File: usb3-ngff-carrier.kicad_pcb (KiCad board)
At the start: 4 copper layers, 90 x 40 mm, 51 parts, among them J1 692221030100, J2 2199119-3, J3 Jack-DC, J4 693043020611, J5 Conn_01x03_Male, SW1 KMR221GLFS, U1 TPS82130SILR

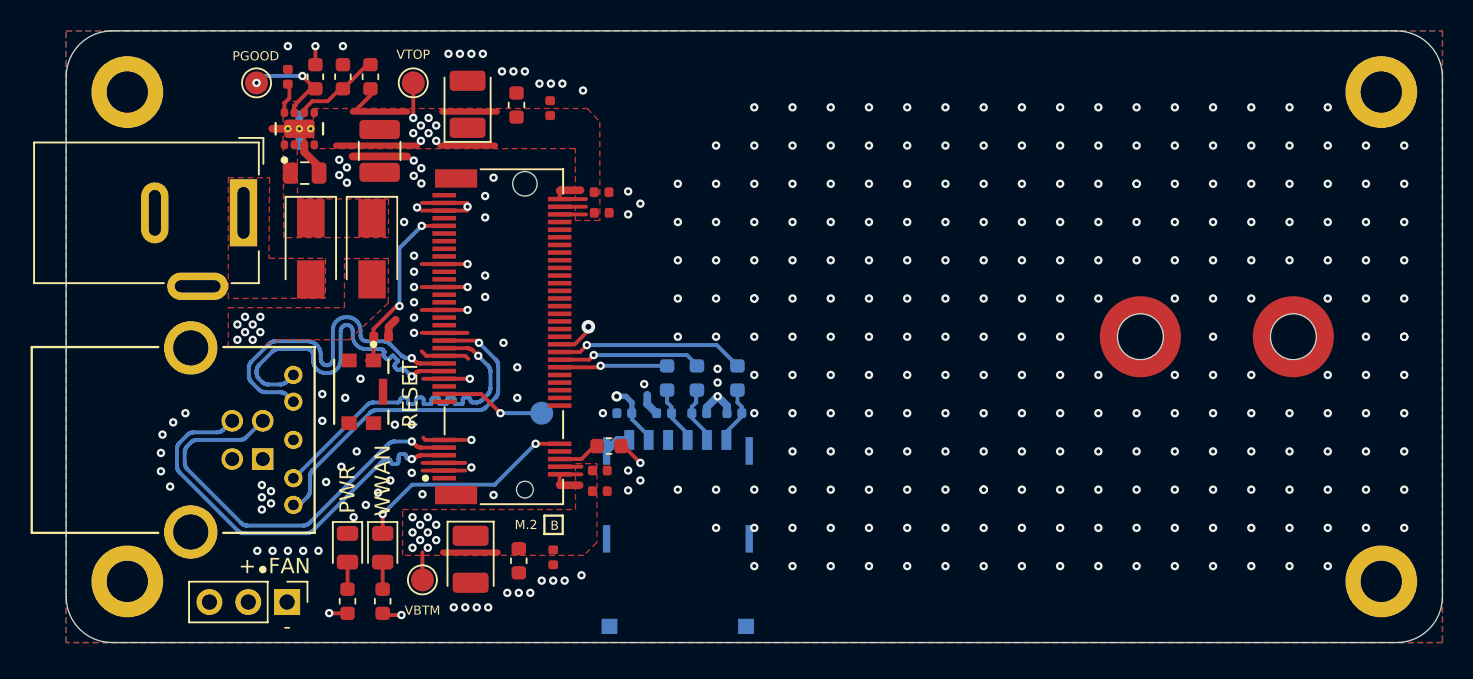
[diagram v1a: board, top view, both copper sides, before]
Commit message: Add: Rev2 changes
* Changed switcher to Diodes Inc device.
* Added second USIM slot and changed USIM slot part.
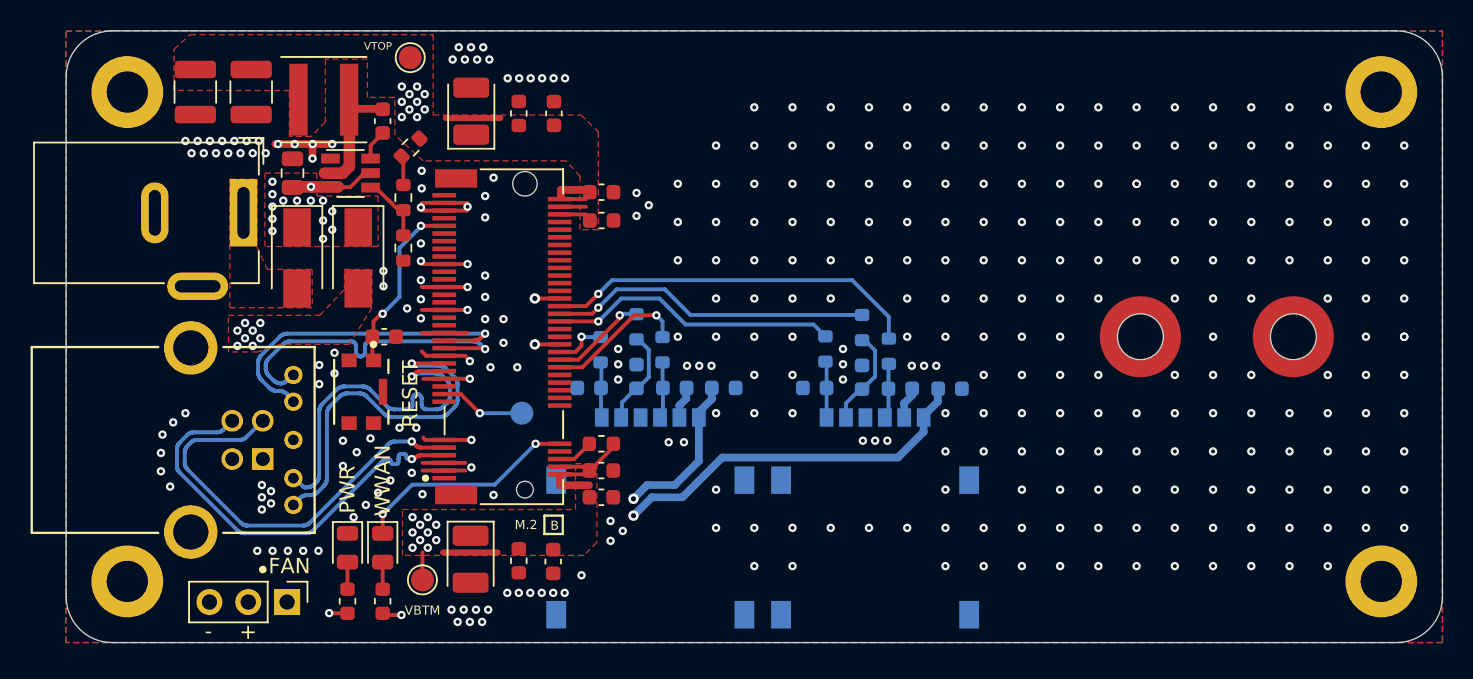
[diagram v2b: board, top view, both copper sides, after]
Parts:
- removed TP3: PGOOD, TestPoint:TestPoint_Pad_D1.5mm
- added C15: 22uF, Capacitor_SMD:C_1210_3225Metric, F.Cu at (12.1, 4.00)
- added C20: 100nF, Capacitor_SMD:C_0603_1608Metric, B.Cu at (43.0, 23.4)
- added C21: 33pF, Capacitor_SMD:C_0603_1608Metric, B.Cu at (39.8, 23.4)
- added C22: 33pF, Capacitor_SMD:C_0603_1608Metric, B.Cu at (37.3, 22.6)
- added C23: 33pF, Capacitor_SMD:C_0603_1608Metric, B.Cu at (34.2, 23.4)
- added J6: SIM8060-6-1-14-00-A, footprint:GCT_SIM8060-6-1-14-00-A, B.Cu at (52.9, 32.1)
- added L1: 3.3uH, Inductor_SMD:L_Coilcraft_XAL5030, F.Cu at (16.9, 4.50)
- added R10: 22R, Resistor_SMD:R_0603_1608Metric, B.Cu at (39.0, 20.9)
- added R11: 22R, Resistor_SMD:R_0603_1608Metric, B.Cu at (37.3, 19.4)
- added R12: 22R, Resistor_SMD:R_0603_1608Metric, B.Cu at (35.0, 20.9)
- C11, C12, C13, C14, C16, C17, C18, C19, C6, C7, C8: footprint Capacitor_SMD:C_0402_1005Metric -> Capacitor_SMD:C_0603_1608Metric
- C2: value 430pF -> 100nF; footprint Capacitor_SMD:C_0402_1005Metric -> Capacitor_SMD:C_0603_1608Metric
- H1, H2: value Threaded Insert -> M2 Threaded Insert
- J4: value 693043020611 -> SIM8060-6-1-14-00-A; footprint footprint:Wurth-693043020611-MFG -> footprint:GCT_SIM8060-6-1-14-00-A
- R2: value 100k -> 0R
- R3: value 374k -> 10k
- R5: value 100k -> 36k5
- U1: value TPS82130SILR -> AP62301WU7; footprint footprint:Texas_Instruments-SIL0008D-0-0-0 -> Package_TO_SOT_SMD:TSOT-23-6
- moved C16 21.4 mm to (57.8, 23.4), turned to 0 degrees
- moved R6 12.7 mm to (53.8, 20.9)
- moved C3 12.7 mm to (8.45, 4.00)
- moved R3 11.4 mm to (22.1, 14.2), turned to 270 degrees
- moved C17 11.0 mm to (54.5, 23.4), turned to 0 degrees
- moved C18 10.9 mm to (52.0, 22.6), turned to 90 degrees
- moved R8 10.5 mm to (49.6, 20.8)
- moved C19 9.99 mm to (49.0, 23.4)
- moved R5 8.83 mm to (22.1, 10.9)
- moved R7 8.79 mm to (52.0, 19.4)
- moved R2 7.76 mm to (22.5, 7.62), turned to 225 degrees
- moved C2 6.84 mm to (20.7, 5.90), turned to 90 degrees
- moved U1 4.43 mm to (18.6, 9.30), turned to 0 degrees
- moved J4 2.04 mm to (38.2, 32.1)
- moved TP1 1.66 mm to (22.5, 1.75)
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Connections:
- net /AP2SDX_STATUS renamed Net-(J2-Pad68)
- net /CONFIG_0 renamed Net-(J2-Pad21)
- net /CONFIG_1 renamed Net-(J2-Pad69)
- net /CONFIG_2 renamed Net-(J2-Pad75)
- net /CONFIG_3 renamed Net-(J2-Pad1)
- net /PCIE_RX_N renamed Net-(J2-Pad47)
- net /PCIE_RX_P renamed Net-(J2-Pad49)
- net /PCIE_TX_N renamed Net-(J2-Pad41)
- net /PCIE_TX_P renamed Net-(J2-Pad43)
- net /REFE_VIO_1V8 renamed /RFFE_VIO_1V8
- net /USIM1_DET renamed Net-(J2-Pad66)
- C16 pad 1: /USIM1_VDD -> /USIM2_VDD
- C2 pad 1: GND -> Net-(C2-Pad1)
- C2 pad 2: Net-(C2-Pad2) -> /SW
- J2 pad 29: /USB_SS_TX_N -> /USB_SS_RX_N
- J2 pad 31: /USB_SS_TX_P -> /USB_SS_RX_P
- J2 pad 35: /USB_SS_RX_N -> /USB_SS_TX_N
- J2 pad 37: /USB_SS_RX_P -> /USB_SS_TX_P
- J2 pad 42: Net-(J2-Pad42) -> /USIM2_DATA
- J2 pad 44: Net-(J2-Pad44) -> /USIM2_CLK
- J2 pad 46: Net-(J2-Pad46) -> /USIM2_RST
- J2 pad 48: Net-(J2-Pad48) -> /USIM2_VDD
- J4 pad C2: Net-(C19-Pad1) -> Net-(C21-Pad1)
- J4 pad C3: Net-(C18-Pad1) -> Net-(C22-Pad1)
- J4 pad C7: Net-(C17-Pad1) -> Net-(C23-Pad1)
- R3 pad 1: +3V8 -> Net-(R3-Pad1)
- R3 pad 2: Net-(R3-Pad2) -> GND
- R5 pad 1: GND -> Net-(R2-Pad2)
- R5 pad 2: Net-(R3-Pad2) -> Net-(R3-Pad1)
- R6 pad 1: Net-(C18-Pad1) -> Net-(C17-Pad1)
- R6 pad 2: /USIM1_CLK -> /USIM2_RST
- R7 pad 1: Net-(C17-Pad1) -> Net-(C18-Pad1)
- R7 pad 2: /USIM1_DATA -> /USIM2_CLK
- R8 pad 2: /USIM1_RST -> /USIM2_DATA
- U1 pad 1: VSYS -> GND
- U1 pad 2: VSYS -> /SW
- U1 pad 3: GND -> VSYS
- U1 pad 4: +3V8 -> Net-(R3-Pad1)
- U1 pad 5: +3V8 -> VSYS
- U1 pad 6: Net-(R3-Pad2) -> Net-(C2-Pad1)
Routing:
- net /USIM2_VDD: track 0.00 -> 43.8 mm, vias 0 -> 2
- net /USIM2_RST: track 0.00 -> 24.6 mm, vias 0 -> 1
- net /USIM2_CLK: track 0.00 -> 21.1 mm, vias 0 -> 1
- net /USIM2_DATA: track 0.00 -> 18.4 mm, vias 0 -> 1
- net +3V8: track 42.6 -> 27.4 mm
- net /USIM1_VDD: track 11.0 -> 24.8 mm
- net GND: track 52.1 -> 41.7 mm, vias 335 -> 342
- net /USIM1_DATA: track 11.8 -> 2.88 mm
- net /SW: track 0.00 -> 6.55 mm
- net Net-(C22-Pad1): track 0.00 -> 5.81 mm
- net VSYS: track 0.00 -> 5.49 mm, vias 0 -> 14
- net Net-(R3-Pad2): track 5.44 -> 0.00 mm
- net Net-(R2-Pad2): track 6.68 -> 1.68 mm, vias 2 -> 0
- net Net-(R3-Pad1): track 0.00 -> 4.08 mm
- net Net-(C23-Pad1): track 0.00 -> 3.15 mm
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- added copper zone on In1.CuPwr, net VSYS
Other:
- board text added: "ISS. B"
- board text added: "USIM 1"
- board text added: "USIM 2"
- board text removed: "4FF USIM"
- board text removed: "ISS. A"
